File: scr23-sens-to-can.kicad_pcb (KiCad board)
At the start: 2 copper layers, 78.7 x 42.9 mm, 65 parts, among them IC1 ADS1256IDBRG4, J1 ATM13-12PA-BM01, J2 6473711-1, SW1 SW_SPDT, U1 SRV05-4, U10 AP63205WU, U2 MCP6004, U3 MCP6004, U4 TJA1042T-3, U5 AP7370-33Y-13, U8 STM32G431CBT6, U9 SRV05-4

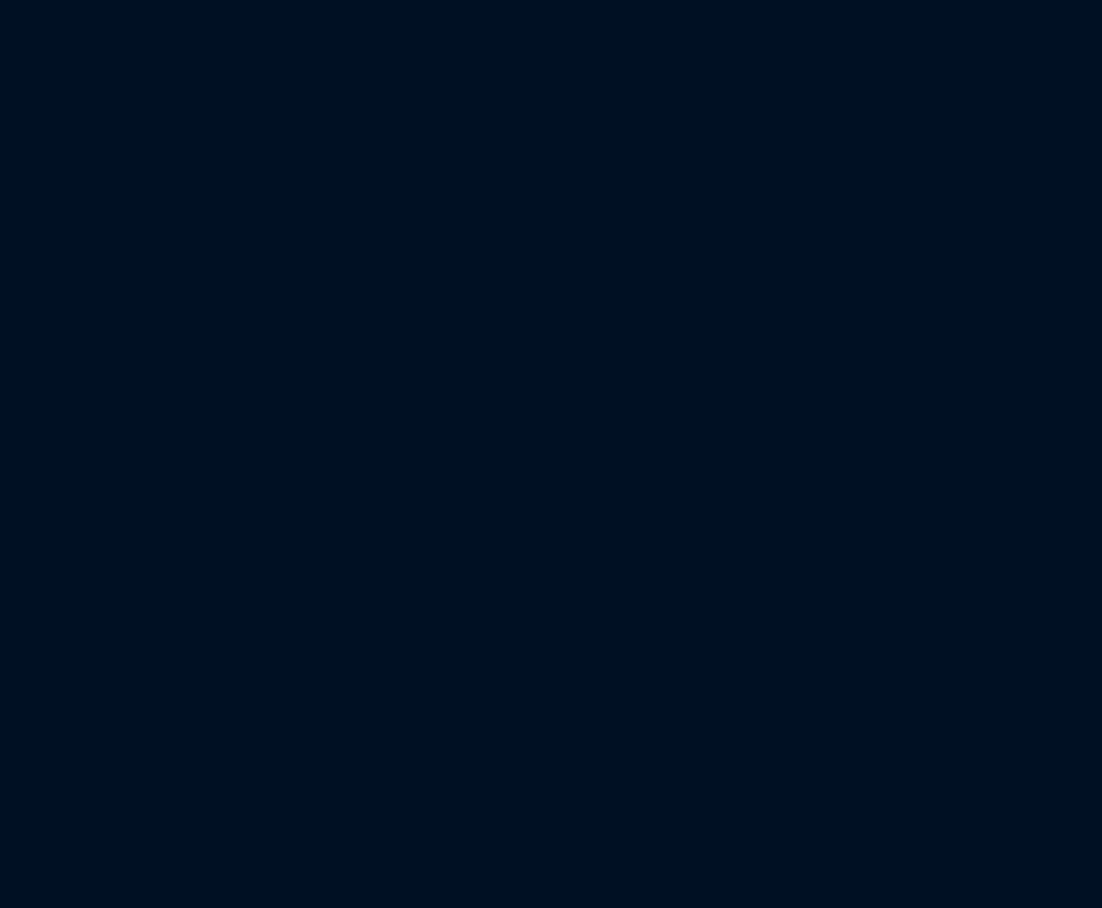
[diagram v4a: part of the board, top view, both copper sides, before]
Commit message: added 34 pin connector, gonna add two CAN transceivers and switch to g474
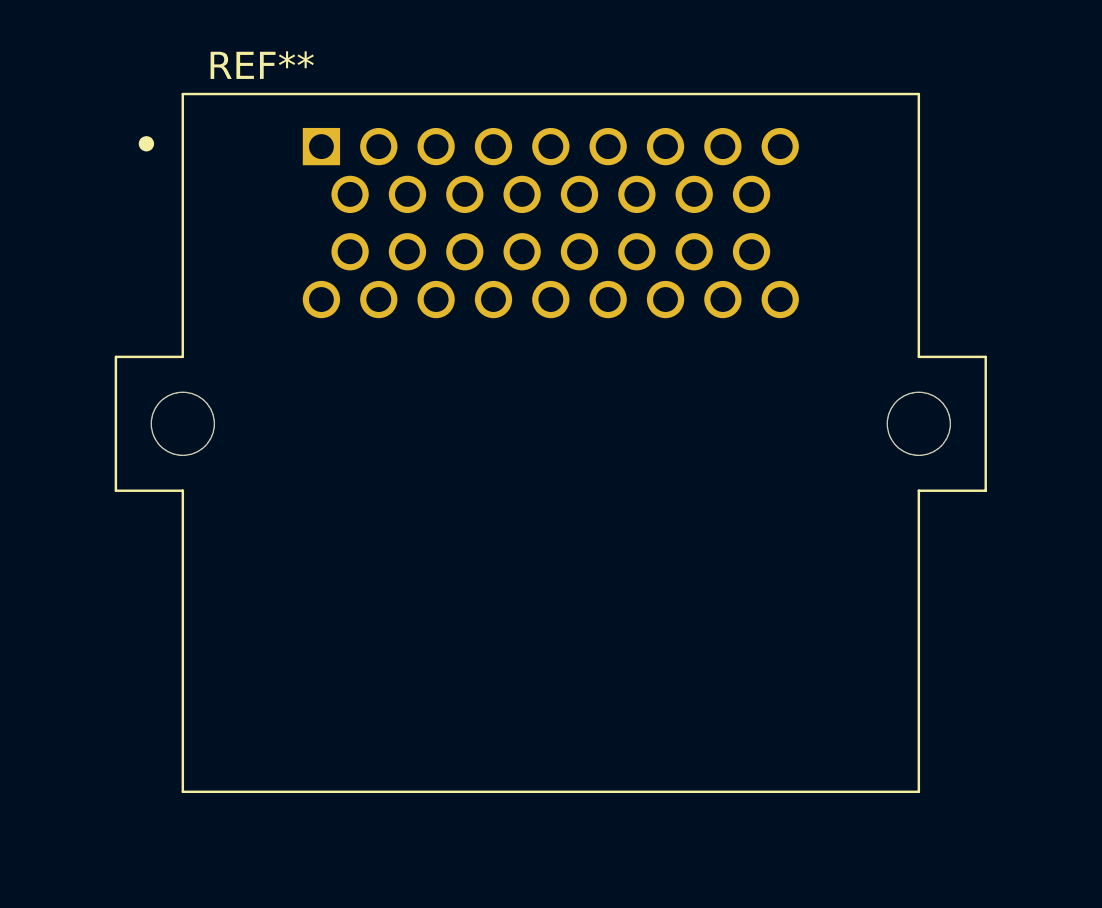
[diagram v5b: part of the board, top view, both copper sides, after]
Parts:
- added REF**: TE_6437288-2, 6437288-2:TE_6437288-2, F.Cu at (210.8, 68.6)
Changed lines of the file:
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@@
+    )
+  )
+  (footprint "6437288-2:TE_6437288-2" (layer "F.Cu")
+    (at 210.82 68.58)
+    (attr through_hole)
+    (fp_text reference "REF**" (at -15.163125 -8.199165) (layer "F.SilkS")
+        (effects (font (size 1.419929 1.419929) (thickness 0.15)))
+    )
+    (fp_text value "TE_6437288-2" (at -8.79134 31.076745) (layer "F.Fab")
+        (effects (font (size 1.419929 1.419929) (thickness 0.15)))
+    )
+    (fp_line (start -22.75 7) (end -22.75 14)
+      (stroke (width 0.127) (type solid)) (layer "F.SilkS"))
+    (fp_line (start -22.75 14) (end -19.25 14)
+      (stroke (width 0.127) (type solid)) (layer "F.SilkS"))
+    (fp_line (start -19.2526 -6.74756) (end -19.2526 7)
+      (stroke (width 0.127) (type solid)) (layer "F.SilkS"))
+    (fp_line (start -19.2526 7) (end -22.75 7)
+      (stroke (width 0.127) (type solid)) (layer "F.SilkS"))
+    (fp_line (start -19.25 14) (end -19.25 29.75)
+      (stroke (width 0.127) (type solid)) (layer "F.SilkS"))
+    (fp_line (start -19.25 29.75) (end 19.25 29.75)
+      (stroke (width 0.127) (type solid)) (layer "F.SilkS"))
+    (fp_line (start 19.25 -6.75) (end -19.25 -6.75)
+      (stroke (width 0.127) (type solid)) (layer "F.SilkS"))
+    (fp_line (start 19.25 7) (end 19.25 -6.75)
+      (stroke (width 0.127) (type solid)) (layer "F.SilkS"))
+    (fp_line (start 19.25 14) (end 22.75 14)
+      (stroke (width 0.127) (type solid)) (layer "F.SilkS"))
+    (fp_line (start 19.25 29.75) (end 19.25 14)
+      (stroke (width 0.127) (type solid)) (layer "F.SilkS"))
+    (fp_line (start 22.75 7) (end 19.25 7)
+      (stroke (width 0.127) (type solid)) (layer "F.SilkS"))
+    (fp_line (start 22.75 14) (end 22.75 7)
+      (stroke (width 0.127) (type solid)) (layer "F.SilkS"))
+    (fp_circle (center -21.1545 -4.148) (end -20.9545 -4.148)
+      (stroke (width 0.4) (type solid)) (fill none) (layer "F.SilkS"))
+    (fp_line (start -23 6.75) (end -23 14.25)
+      (stroke (width 0.05) (type solid)) (layer "F.CrtYd"))
+    (fp_line (start -23 14.25) (end -19.5 14.25)
+      (stroke (width 0.05) (type solid)) (layer "F.CrtYd"))
+    (fp_line (start -19.5 -7) (end -19.5 6.75)
+      (stroke (width 0.05) (type solid)) (layer "F.CrtYd"))
+    (fp_line (start -19.5 6.75) (end -23 6.75)
+      (stroke (width 0.05) (type solid)) (layer "F.CrtYd"))
+    (fp_line (start -19.5 14.25) (end -19.5 30)
+      (stroke (width 0.05) (type solid)) (layer "F.CrtYd"))
+    (fp_line (start -19.5 30) (end 19.5 30)
+      (stroke (width 0.05) (type solid)) (layer "F.CrtYd"))
+    (fp_line (start 19.5 -7) (end -19.5 -7)
+      (stroke (width 0.05) (type solid)) (layer "F.CrtYd"))
+    (fp_line (start 19.5 6.75) (end 19.5 -7)
+      (stroke (width 0.05) (type solid)) (layer "F.CrtYd"))
+    (fp_line (start 19.5 14.25) (end 23 14.25)
+      (stroke (width 0.05) (type solid)) (layer "F.CrtYd"))
+    (fp_line (start 19.5 30) (end 19.5 14.25)
+      (stroke (width 0.05) (type solid)) (layer "F.CrtYd"))
+    (fp_line (start 23 6.75) (end 19.5 6.75)
+      (stroke (width 0.05) (type solid)) (layer "F.CrtYd"))
+    (fp_line (start 23 14.25) (end 23 6.75)
+      (stroke (width 0.05) (type solid)) (layer "F.CrtYd"))
+    (fp_line (start -22.75 7) (end -22.75 14)
+      (stroke (width 0.127) (type solid)) (layer "F.Fab"))
+    (fp_line (start -22.75 14) (end -19.25 14)
+      (stroke (width 0.127) (type solid)) (layer "F.Fab"))
+    (fp_line (start -19.25 -6.75) (end -19.25 7)
+      (stroke (width 0.127) (type solid)) (layer "F.Fab"))
+    (fp_line (start -19.25 7) (end -22.75 7)
+      (stroke (width 0.127) (type solid)) (layer "F.Fab"))
+    (fp_line (start -19.25 14) (end -19.25 29.75)
+      (stroke (width 0.127) (type solid)) (layer "F.Fab"))
+    (fp_line (start -19.25 29.75) (end 19.25 29.75)
+      (stroke (width 0.127) (type solid)) (layer "F.Fab"))
+    (fp_line (start 19.25 -6.75) (end -19.25 -6.75)
+      (stroke (width 0.127) (type solid)) (layer "F.Fab"))
+    (fp_line (start 19.25 7) (end 19.25 -6.75)
+      (stroke (width 0.127) (type solid)) (layer "F.Fab"))
+    (fp_line (start 19.25 7) (end 22.75 7)
+      (stroke (width 0.127) (type solid)) (layer "F.Fab"))
+    (fp_line (start 19.25 29.75) (end 19.25 14)
+      (stroke (width 0.127) (type solid)) (layer "F.Fab"))
+    (fp_line (start 22.75 7) (end 22.75 14)
+      (stroke (width 0.127) (type solid)) (layer "F.Fab"))
+    (fp_line (start 22.75 14) (end 19.25 14)
+      (stroke (width 0.127) (type solid)) (layer "F.Fab"))
+    (fp_circle (center -21.1545 -4.148) (end -20.9545 -4.148)
+      (stroke (width 0.4) (type solid)) (fill none) (layer "F.Fab"))
+    (pad "" np_thru_hole circle (at -19.25 10.5) (size 3.3 3.3) (drill 3.3) (layers "*.Cu" "*.Mask"))
+    (pad "" np_thru_hole circle (at 19.25 10.5) (size 3.3 3.3) (drill 3.3) (layers "*.Cu" "*.Mask"))
+    (pad "1" thru_hole rect (at -12 -4) (size 1.95 1.95) (drill 1.3) (layers "*.Cu" "*.Mask")
+      (solder_mask_margin 0.102))
+    (pad "2" thru_hole circle (at -9 -4) (size 1.95 1.95) (drill 1.3) (layers "*.Cu" "*.Mask")
+      (solder_mask_margin 0.102))
+    (pad "3" thru_hole circle (at -6 -4) (size 1.95 1.95) (drill 1.3) (layers "*.Cu" "*.Mask")
+      (solder_mask_margin 0.102))
+    (pad "4" thru_hole circle (at -3 -4) (size 1.95 1.95) (drill 1.3) (layers "*.Cu" "*.Mask")
+      (solder_mask_margin 0.102))
+    (pad "5" thru_hole circle (at 0 -4) (size 1.95 1.95) (drill 1.3) (layers "*.Cu" "*.Mask")
+      (solder_mask_margin 0.102))
+    (pad "6" thru_hole circle (at 3 -4) (size 1.95 1.95) (drill 1.3) (layers "*.Cu" "*.Mask")
+      (solder_mask_margin 0.102))
+    (pad "7" thru_hole circle (at 6 -4) (size 1.95 1.95) (drill 1.3) (layers "*.Cu" "*.Mask")
+      (solder_mask_margin 0.102))
+    (pad "8" thru_hole circle (at 9 -4) (size 1.95 1.95) (drill 1.3) (layers "*.Cu" "*.Mask")
+      (solder_mask_margin 0.102))
+    (pad "9" thru_hole circle (at 12 -4) (size 1.95 1.95) (drill 1.3) (layers "*.Cu" "*.Mask")
+      (solder_mask_margin 0.102))
+    (pad "10" thru_hole circle (at -10.5 -1.5) (size 1.95 1.95) (drill 1.3) (layers "*.Cu" "*.Mask")
+      (solder_mask_margin 0.102))
+    (pad "11" thru_hole circle (at -7.5 -1.5) (size 1.95 1.95) (drill 1.3) (layers "*.Cu" "*.Mask")
+      (solder_mask_margin 0.102))
+    (pad "12" thru_hole circle (at -4.5 -1.5) (size 1.95 1.95) (drill 1.3) (layers "*.Cu" "*.Mask")
+      (solder_mask_margin 0.102))
+    (pad "13" thru_hole circle (at -1.5 -1.5) (size 1.95 1.95) (drill 1.3) (layers "*.Cu" "*.Mask")
+      (solder_mask_margin 0.102))
+    (pad "14" thru_hole circle (at 1.5 -1.5) (size 1.95 1.95) (drill 1.3) (layers "*.Cu" "*.Mask")
+      (solder_mask_margin 0.102))
+    (pad "15" thru_hole circle (at 4.5 -1.5) (size 1.95 1.95) (drill 1.3) (layers "*.Cu" "*.Mask")
+      (solder_mask_margin 0.102))
+    (pad "16" thru_hole circle (at 7.5 -1.5) (size 1.95 1.95) (drill 1.3) (layers "*.Cu" "*.Mask")
+      (solder_mask_margin 0.102))
+    (pad "17" thru_hole circle (at 10.5 -1.5) (size 1.95 1.95) (drill 1.3) (layers "*.Cu" "*.Mask")
+      (solder_mask_margin 0.102))
+    (pad "18" thru_hole circle (at -10.5 1.5) (size 1.95 1.95) (drill 1.3) (layers "*.Cu" "*.Mask")
+      (solder_mask_margin 0.102))
+    (pad "19" thru_hole circle (at -7.5 1.5) (size 1.95 1.95) (drill 1.3) (layers "*.Cu" "*.Mask")
+      (solder_mask_margin 0.102))
+    (pad "20" thru_hole circle (at -4.5 1.5) (size 1.95 1.95) (drill 1.3) (layers "*.Cu" "*.Mask")
+      (solder_mask_margin 0.102))
+    (pad "21" thru_hole circle (at -1.5 1.5) (size 1.95 1.95) (drill 1.3) (layers "*.Cu" "*.Mask")
+      (solder_mask_margin 0.102))
+    (pad "22" thru_hole circle (at 1.5 1.5) (size 1.95 1.95) (drill 1.3) (layers "*.Cu" "*.Mask")
+      (solder_mask_margin 0.102))
+    (pad "23" thru_hole circle (at 4.5 1.5) (size 1.95 1.95) (drill 1.3) (layers "*.Cu" "*.Mask")
+      (solder_mask_margin 0.102))
+    (pad "24" thru_hole circle (at 7.5 1.5) (size 1.95 1.95) (drill 1.3) (layers "*.Cu" "*.Mask")
+      (solder_mask_margin 0.102))
+    (pad "25" thru_hole circle (at 10.5 1.5) (size 1.95 1.95) (drill 1.3) (layers "*.Cu" "*.Mask")
+      (solder_mask_margin 0.102))
+    (pad "26" thru_hole circle (at -12 4) (size 1.95 1.95) (drill 1.3) (layers "*.Cu" "*.Mask")
+      (solder_mask_margin 0.102))
+    (pad "27" thru_hole circle (at -9 4) (size 1.95 1.95) (drill 1.3) (layers "*.Cu" "*.Mask")
+      (solder_mask_margin 0.102))
+    (pad "28" thru_hole circle (at -6 4) (size 1.95 1.95) (drill 1.3) (layers "*.Cu" "*.Mask")
+      (solder_mask_margin 0.102))
+    (pad "29" thru_hole circle (at -3 4) (size 1.95 1.95) (drill 1.3) (layers "*.Cu" "*.Mask")
+      (solder_mask_margin 0.102))
+    (pad "30" thru_hole circle (at 0 4) (size 1.95 1.95) (drill 1.3) (layers "*.Cu" "*.Mask")
+      (solder_mask_margin 0.102))
+    (pad "31" thru_hole circle (at 3 4) (size 1.95 1.95) (drill 1.3) (layers "*.Cu" "*.Mask")
+      (solder_mask_margin 0.102))
+    (pad "32" thru_hole circle (at 6 4) (size 1.95 1.95) (drill 1.3) (layers "*.Cu" "*.Mask")
+      (solder_mask_margin 0.102))
+    (pad "33" thru_hole circle (at 9 4) (size 1.95 1.95) (drill 1.3) (layers "*.Cu" "*.Mask")
+      (solder_mask_margin 0.102))
+    (pad "34" thru_hole circle (at 12 4) (size 1.95 1.95) (drill 1.3) (layers "*.Cu" "*.Mask")
+      (solder_mask_margin 0.102))
+    (model "${KIPRJMOD}/6437288-2/6437288-2.step"
+      (offset (xyz 0 -30 14))
+      (scale (xyz 1 1 1))
+      (rotate (xyz -90 0 0))
     )
   )

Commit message: finish layout mk1
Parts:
- removed J1: ATM13-12PA-BM01, scr23-sens-to-can-main:ATM1312PABM01
- removed R11, R13, R17: 1370, Resistor_SMD:R_0603_1608Metric
- removed R12, R14, R18, R8: 2670, Resistor_SMD:R_0603_1608Metric
- removed REF**: TE_6437288-2, 6437288-2:TE_6437288-2
- added C30: 27pF, Capacitor_SMD:C_0603_1608Metric_Pad1.08x0.95mm_HandSolder, F.Cu at (137.0, 86.7)
- added C31: 27pF, Capacitor_SMD:C_0603_1608Metric_Pad1.08x0.95mm_HandSolder, F.Cu at (137.0, 89.2)
- added C32: TCP0J106M8R, Capacitor_SMD:C_0805_2012Metric, F.Cu at (115.8, 90.4)
- added C33: 100n, Capacitor_SMD:C_0805_2012Metric, F.Cu at (129.3, 106.5)
- added C34: 100pF, Capacitor_SMD:C_0805_2012Metric, F.Cu at (127.5, 70.7)
- added J3: Conn_ST_STDC14, Connector_PinHeader_1.27mm:PinHeader_2x07_P1.27mm_Vertical_SMD, F.Cu at (126.0, 118.6)
- added J4: 6437288-2, 6437288-2:TE_6437288-2, F.Cu at (139.8, 136.6)
- added Y3: ECS-76.8-18-5PXEN-TR, ECS_76_8_18_5PXEN_TR:XTAL_ECS-76.8-18-5PXEN-TR, F.Cu at (132.6, 88.4)
- C28: value 100uF -> TCP0J106M8R
- C29: value 100uF -> 1u
- L1: value 4.7uH -> 10uH
- R1: value 1370 -> 100
- R15: value 1k -> 221k
- R2: value 2670 -> 330
- R3: value 1370 -> 0; footprint Resistor_SMD:R_0603_1608Metric -> Resistor_SMD:R_0603_1608Metric_Pad0.98x0.95mm_HandSolder
- R4: value 2670 -> 0; footprint Resistor_SMD:R_0603_1608Metric -> Resistor_SMD:R_0603_1608Metric_Pad0.98x0.95mm_HandSolder
- R5: value 1370 -> 33k
- R6: value 2670 -> 10k
- R7: value 1370 -> 50k
- U2: value MCP6004 -> SRV05-4; footprint MCP6004T-I_ST:SOP65P640X120-14N -> Package_TO_SOT_SMD:SOT-23-6
- U3: value MCP6004 -> LM4040DCK-2.5; footprint MCP6004T-I_ST:SOP65P640X120-14N -> Package_TO_SOT_SMD:SOT-353_SC-70-5
- moved J2 127.5 mm to (99.1, 72.7), turned to -90 degrees
- moved FB2 114.6 mm to (118.1, 90.7), turned to 90 degrees
- moved IC1 103.8 mm to (123.9, 99.0)
- moved C29 88.8 mm to (127.0, 106.5), turned to 90 degrees
- moved H1 79.0 mm to (92.5, 119.9)
- moved C2 58.5 mm to (110.0, 73.5), turned to 90 degrees
- moved C24 56.1 mm to (110.0, 69.7)
- moved C10 53.7 mm to (105.7, 85.1), turned to 180 degrees
- moved H2 50.0 mm to (92.5, 68.3)
- moved U9 49.4 mm to (106.3, 105.5), turned to 180 degrees
- moved U10 48.2 mm to (113.6, 69.2), turned to 0 degrees
- moved D1 47.9 mm to (117.6, 74.3), turned to -90 degrees
- moved C5 45.8 mm to (118.6, 106.7), turned to -90 degrees
- moved C16 45.5 mm to (113.0, 90.4), turned to -90 degrees
- moved H4 44.7 mm to (157.5, 119.9)
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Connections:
- C26 pad 1: +5V -> +6V
- C27 pad 1: +5V -> +6V
- C29 pad 1: GND -> +3.3VA
- C29 pad 2: +5VA -> GND
- D1 pad 2: Net-(D1-A) -> +6V
- FB1 pad 1: +3.3V -> Net-(FB1-Pad1)
- FB2 pad 2: +5VA -> Net-(FB2-Pad2)
- IC1 pad 14: unconnected-(IC1-~{SYNC_}PDWN-Pad14) -> +3.3V
- IC1 pad 15: unconnected-(IC1-~{RESET}-Pad15) -> +3.3V
- IC1 pad 16: unconnected-(IC1-DVDD-Pad16) -> +3.3V
- IC1 pad 17: unconnected-(IC1-DGND-Pad17) -> GND
- IC1 pad 18: unconnected-(IC1-XTAL2-Pad18) -> /XTAL2
- IC1 pad 19: unconnected-(IC1-XTAL1/CLKIN-Pad19) -> /XTAL1
- IC1 pad 20: unconnected-(IC1-~{CS}-Pad20) -> /ADC_CS
- IC1 pad 21: unconnected-(IC1-~{DRDY}-Pad21) -> /DATA_RDY
- IC1 pad 22: unconnected-(IC1-DOUT-Pad22) -> /SPI1_MISO
- IC1 pad 23: unconnected-(IC1-DIN-Pad23) -> /SPI1_MOSI
- IC1 pad 24: unconnected-(IC1-SCLK-Pad24) -> /SPI1_SCK
- IC1 pad 4: +5VA -> +2V5
- J2 pad 10: unconnected-(J2-Pad10) -> A2
- J2 pad 11: unconnected-(J2-Pad11) -> A3
- J2 pad 12: unconnected-(J2-Pad12) -> D0
- J2 pad 13: unconnected-(J2-Pad13) -> D1
- J2 pad 16: unconnected-(J2-Pad16) -> +5V
- J2 pad 17: unconnected-(J2-Pad17) -> +5V
- J2 pad 18: unconnected-(J2-Pad18) -> +5V
- J2 pad 19: unconnected-(J2-Pad19) -> +5V
- J2 pad 20: unconnected-(J2-Pad20) -> +5V
- J2 pad 21: unconnected-(J2-Pad21) -> A4
- J2 pad 22: unconnected-(J2-Pad22) -> A5
- J2 pad 23: unconnected-(J2-Pad23) -> A6
- J2 pad 24: unconnected-(J2-Pad24) -> A7
- J2 pad 25: unconnected-(J2-Pad25) -> D2
- J2 pad 26: unconnected-(J2-Pad26) -> D3
- J2 pad 3: unconnected-(J2-Pad3) -> GND
- J2 pad 4: unconnected-(J2-Pad4) -> GND
- J2 pad 5: unconnected-(J2-Pad5) -> GND
- J2 pad 6: unconnected-(J2-Pad6) -> GND
- J2 pad 7: unconnected-(J2-Pad7) -> GND
- J2 pad 8: unconnected-(J2-Pad8) -> A0
- J2 pad 9: unconnected-(J2-Pad9) -> A1
- L1 pad 2: +5V -> +6V
- R1 pad 1: A0 -> GND
- R1 pad 2: Net-(U2A-+) -> Net-(J3-GNDDetect)
- R15 pad 1: +5V -> +6V
- R15 pad 2: Net-(D1-A) -> Net-(U10-FB)
- R2 pad 1: Net-(U2A-+) -> +5V
- R2 pad 2: GND -> +2V5
- R3 pad 1: A1 -> +5VA
- R3 pad 2: Net-(U2B-+) -> Net-(FB2-Pad2)
- R4 pad 1: Net-(U2B-+) -> Net-(FB1-Pad1)
- R4 pad 2: GND -> +3.3V
- R5 pad 1: A2 -> Net-(U10-FB)
- R5 pad 2: Net-(U2C-+) -> GND
- R6 pad 1: Net-(U2C-+) -> +6V
- R6 pad 2: GND -> +5V
- R7 pad 1: A3 -> +5V
- R7 pad 2: Net-(U2D-+) -> GND
- U10 pad 1: +5V -> Net-(U10-FB)
- U2 pad 1: ADC1_IN1 -> D0
- U2 pad 2: ADC1_IN1 -> GND
- U2 pad 3: Net-(U2A-+) -> D1
- U2 pad 4: +3.3V -> D2
- U2 pad 5: Net-(U2B-+) -> +5V
- U2 pad 6: ADC1_IN2 -> D3
- U3 pad 1: ADC2_IN13 -> GND
- U3 pad 2: ADC2_IN13 -> (no net)
- U3 pad 3: Net-(U3A-+) -> +2V5
- U3 pad 4: +3.3V -> (no net)
- U3 pad 5: Net-(U3B-+) -> (no net)
- U8 pad 10: D1 -> unconnected-(U8A-PA2-Pad10)
- U8 pad 11: unconnected-(U8A-PA3-Pad11) -> /DATA_RDY
- U8 pad 12: unconnected-(U8A-PA4-Pad12) -> /ADC_CS
- U8 pad 13: SPI1_SCK -> /SPI1_SCK
- U8 pad 14: SPI1_MISO -> /SPI1_MISO
- U8 pad 15: SPI1_MOSI -> /SPI1_MOSI
- U8 pad 20: unconnected-(U8B-VREF+-Pad20) -> +3.3VA
- U8 pad 24: +3.3V -> Net-(FB1-Pad1)
- U8 pad 25: USB_DM -> D0
- U8 pad 26: USB_DP -> D1
- U8 pad 29: unconnected-(U8A-PB15-Pad29) -> D2
- U8 pad 30: unconnected-(U8A-PA8-Pad30) -> D3
- U8 pad 36: +3.3V -> Net-(FB1-Pad1)
- U8 pad 48: +3.3V -> Net-(FB1-Pad1)
- U8 pad 7: unconnected-(U8A-PG10-NRST-Pad7) -> /NRST
- U8 pad 9: D0 -> unconnected-(U8A-PA1-Pad9)
- U9 pad 6: unconnected-(U9-IO4-Pad6) -> A7
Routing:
- net D1: track 0.00 -> 44.1 mm
- net +12V: track 65.3 -> 21.3 mm, vias 2 -> 0
- net D0: track 0.00 -> 42.7 mm, vias 0 -> 2
- net A6: track 60.8 -> 19.9 mm, vias 1 -> 2
- net A3: track 68.2 -> 28.2 mm, vias 1 -> 3
- net Net-(FB1-Pad1): track 0.00 -> 35.3 mm, vias 0 -> 2
- net D3: track 0.00 -> 33.4 mm, vias 0 -> 2
- net D2: track 0.00 -> 31.8 mm, vias 0 -> 2
- net +6V: track 0.00 -> 27.5 mm
- net CANH: track 30.7 -> 57.1 mm, vias 0 -> 2
- net /XTAL1: track 0.00 -> 25.7 mm, vias 0 -> 2
- net Net-(U10-FB): track 0.00 -> 24.7 mm, vias 0 -> 2
- net ADC2_IN4: track 24.0 -> 0.00 mm, vias 2 -> 0
- net /DATA_RDY: track 0.00 -> 23.7 mm, vias 0 -> 2
- net /NRST: track 0.00 -> 22.3 mm, vias 0 -> 2
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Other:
- board size 78.7 x 42.9 mm -> 77.2 x 62.5 mm

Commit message: add LDO
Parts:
- removed R6: 10k, Resistor_SMD:R_0603_1608Metric
- removed R7: 50k, Resistor_SMD:R_0603_1608Metric
- added C35: 2.2uF, Capacitor_SMD:C_0805_2012Metric, F.Cu at (132.2, 65.0)
- added C36: 2.2uF, Capacitor_SMD:C_0805_2012Metric, F.Cu at (142.4, 65.0)
- added U6: ADP7142AUJZ-5.0, Package_TO_SOT_SMD:TSOT-23-5, F.Cu at (137.0, 65.9)
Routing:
- net GND: track 121.2 -> 129.6 mm
- net Net-(U6-EN): track 0.00 -> 6.21 mm

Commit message: component
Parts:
- removed U10: AP63205WU, Package_TO_SOT_SMD:TSOT-23-6
- added U7: AP63200WU, Package_TO_SOT_SMD:TSOT-23-6, F.Cu at (114.2, 69.1)
- R5: value 33k -> 34k
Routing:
- net Net-(U7-FB): track 24.7 -> 27.0 mm
- net +12V: track 21.3 -> 22.0 mm
- net Net-(U7-SW): track 7.32 -> 6.75 mm
- net Net-(U7-BST): track 3.69 -> 3.12 mm
